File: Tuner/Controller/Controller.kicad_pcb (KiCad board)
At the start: 2 copper layers, 96.8 x 99.3 mm, 169 parts, among them J1 Conn_01x06, J10 Conn_01x05, J11 Conn_01x01, J12 Conn_01x02, J14 Conn_01x01, J15 Conn_01x02, J16 Conn_01x06, J17 Conn_01x01, J18 Conn_01x01, J19 Conn_01x01, J2 Conn_01x06, J20 Conn_01x01, J21 Conn_01x01, J22 Conn_01x06, J23 Conn_01x01, J24 Conn_01x01, J25 Conn_01x01, J26 Conn_01x02, J27 Conn_01x02, J28 Conn_01x02, J3 Conn_01x06, J30 Conn_01x02, J4 Conn_01x06, J5 Conn_01x06, J6 Conn_01x06, J7 Conn_01x02, J8 Conn_01x06, J9 Conn_01x06, Q1 2N3904, Q2 2N3904, Q3 2N3904, Q4 2N3904, Q5 2N3904, Q6 2N3904, Q7 2N3904, Q8 2N3904, U1 74LS393, U2 74HC14, U3 74HC86, U4 LM350_TO220

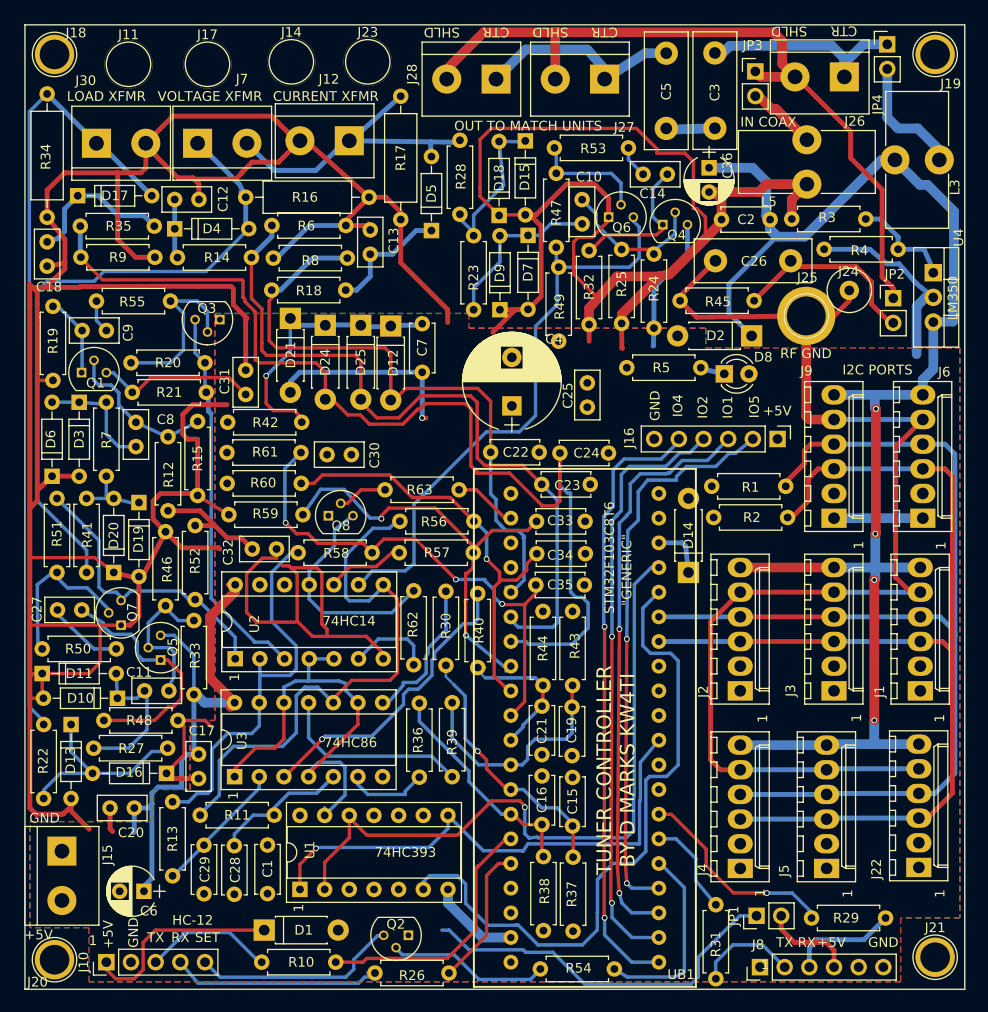
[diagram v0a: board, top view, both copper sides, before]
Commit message: JLCPCB order 09232018 - improved grounding - improved I2C cabling - NEO7M port - support for common mode chokes - relay board now has capacitors on all coils
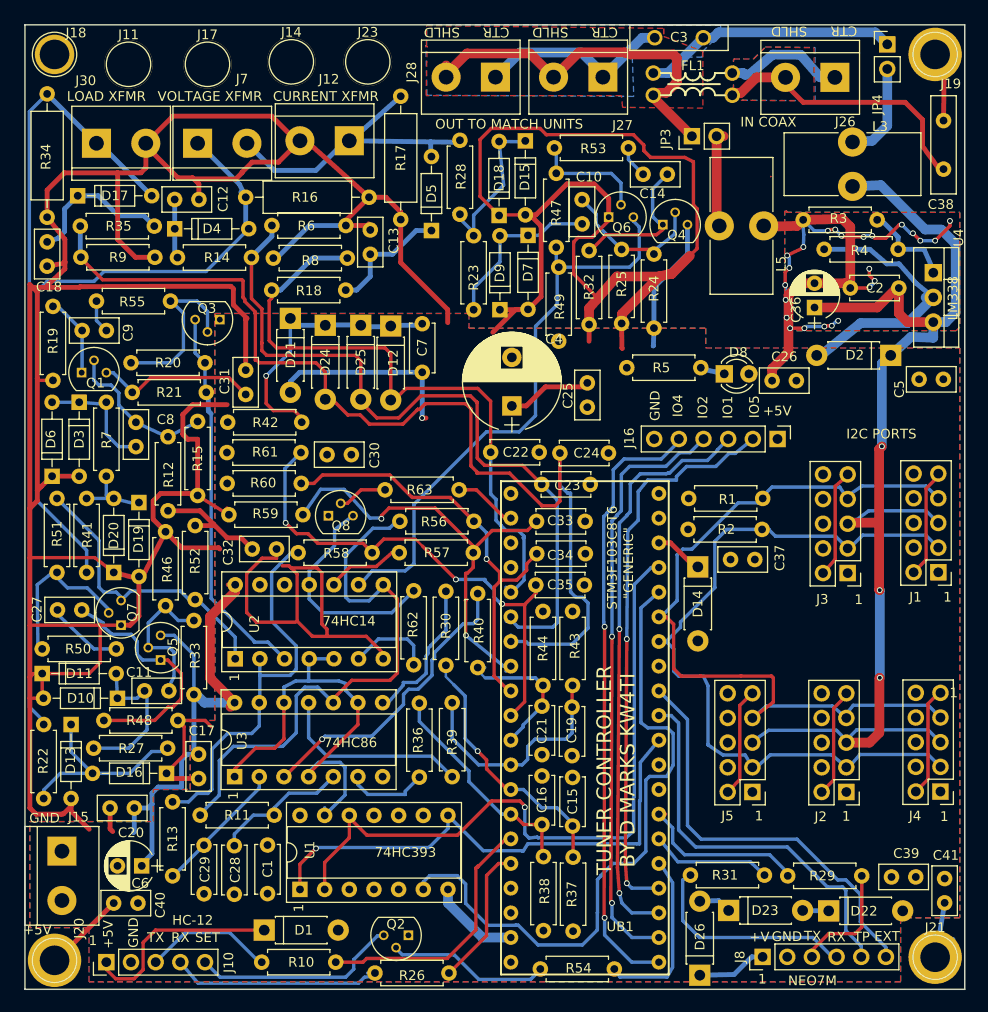
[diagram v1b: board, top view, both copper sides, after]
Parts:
- removed J22, J6, J9: Conn_01x06, Connectors_Molex:Molex_KK-6410-06_06x2.54mm_Straight
- removed J24, J25: Conn_01x01, Connectors:1pin
- removed JP1, JP2: Jumper, Pin_Headers:Pin_Header_Straight_1x02_Pitch2.54mm
- removed R45: 10k, Resistors_THT:R_Axial_DIN0207_L6.3mm_D2.5mm_P7.62mm_Horizontal
- added C37: 0.1 uF, Capacitors_THT:C_Disc_D5.0mm_W2.5mm_P2.50mm, F.Cu at (130.5, 84.0)
- added C38: 0.1 uF, Capacitors_THT:C_Disc_D10.0mm_W2.5mm_P5.00mm, F.Cu at (150.0, 43.8)
- added C39: 0.1 uF, Capacitors_THT:C_Disc_D5.0mm_W2.5mm_P2.50mm, F.Cu at (147.1, 116.7)
- added C40: 0.1 uF, Capacitors_THT:C_Disc_D5.0mm_W2.5mm_P2.50mm, F.Cu at (64.5, 119.4)
- added C41: 0.1 uF, Capacitors_THT:C_Disc_D5.0mm_W2.5mm_P2.50mm, F.Cu at (150.1, 119.4)
- added D22: 1N4001, Diodes_THT:D_DO-41_SOD81_P7.62mm_Horizontal, F.Cu at (138.1, 120.2)
- added D23: 1N4001, Diodes_THT:D_DO-41_SOD81_P7.62mm_Horizontal, F.Cu at (127.8, 120.2)
- added D26: 1N4001, Diodes_THT:D_DO-41_SOD81_P7.62mm_Horizontal, F.Cu at (124.9, 126.8)
- added FL1: Choke, Controller:GenericCMCL, F.Cu at (124.1, 36.5)
- C26, C5: footprint Capacitors_THT:C_Disc_D12.0mm_W4.4mm_P7.75mm -> Capacitors_THT:C_Disc_D5.0mm_W2.5mm_P2.50mm
- C3: footprint Capacitors_THT:C_Disc_D12.0mm_W4.4mm_P7.75mm -> Capacitors_THT:C_Disc_D10.0mm_W2.5mm_P5.00mm
- J1, J2, J3, J4, J5: value Conn_01x06 -> Conn_02x05_Odd_Even; footprint Connectors_Molex:Molex_KK-6410-06_06x2.54mm_Straight -> Pin_Headers:Pin_Header_Straight_2x05_Pitch2.54mm
- moved C5 36.7 mm to (147.4, 65.5), turned to 0 degrees
- moved J4 22.1 mm to (149.6, 107.9), turned to 180 degrees
- moved C36 18.0 mm to (136.7, 58.1), turned to 90 degrees
- moved J2 15.1 mm to (140.0, 108.0), turned to 180 degrees
- moved C2 15.0 mm to (140.4, 56.1)
- moved D2 14.5 mm to (144.5, 63.0)
- moved L5 12.6 mm to (126.9, 49.7), turned to 90 degrees
- moved C26 12.4 mm to (134.8, 65.6)
- moved J1 12.3 mm to (149.4, 85.3), turned to 180 degrees
- moved J3 12.2 mm to (140.1, 85.4), turned to 180 degrees
- moved R31 11.0 mm to (123.9, 116.5), turned to 0 degrees
- moved J5 11.0 mm to (130.3, 108.0), turned to 180 degrees
- moved JP3 9.33 mm to (124.1, 40.4), turned to 90 degrees
- moved L3 9.13 mm to (140.6, 41.0), turned to 0 degrees
- moved R29 4.99 mm to (141.5, 116.6)
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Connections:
- C26 pad 1: Net-(C26-Pad1) -> +5V
- C26 pad 2: RFGND -> GND
- C5 pad 1: Net-(C3-Pad2) -> +5V
- C5 pad 2: Net-(C5-Pad2) -> GND
- J1 pad 4: I2CSDA -> GND
- J1 pad 5: RFGND -> UPWR
- J1 pad 6: UPWR -> GND
- J19 pad 1: (no net) -> Net-(C38-Pad2)
- J2 pad 4: I2CSDA -> GND
- J2 pad 5: RFGND -> UPWR
- J2 pad 6: UPWR -> GND
- J20 pad 1: (no net) -> Net-(C40-Pad1)
- J21 pad 1: (no net) -> Net-(C41-Pad1)
- J26 pad 1: Net-(C3-Pad1) -> Net-(FL1-Pad1)
- J26 pad 2: Net-(J26-Pad2) -> Net-(C38-Pad1)
- J27 pad 1: Net-(C5-Pad2) -> Net-(C3-Pad2)
- J27 pad 2: Net-(J26-Pad2) -> Net-(FL1-Pad4)
- J28 pad 1: Net-(C5-Pad2) -> Net-(C3-Pad2)
- J28 pad 2: Net-(J26-Pad2) -> Net-(FL1-Pad4)
- J3 pad 4: I2CSDA -> GND
- J3 pad 5: RFGND -> UPWR
- J3 pad 6: UPWR -> GND
- J4 pad 4: I2CSDA -> GND
- J4 pad 5: RFGND -> UPWR
- J4 pad 6: UPWR -> GND
- J5 pad 4: I2CSDA -> GND
- J5 pad 5: RFGND -> UPWR
- J5 pad 6: UPWR -> GND
- J8 pad 1: (no net) -> Net-(D26-Pad1)
- J8 pad 2: Net-(J8-Pad2) -> GND
- J8 pad 5: (no net) -> Net-(J8-Pad5)
- J8 pad 6: GND -> Net-(J8-Pad6)
- JP3 pad 1: Net-(J26-Pad2) -> Net-(FL1-Pad4)
- R31 pad 1: Net-(J8-Pad2) -> Net-(J8-Pad4)
- UB1 pad 39: (no net) -> Net-(J8-Pad5)
- UB1 pad 40: (no net) -> Net-(J8-Pad6)
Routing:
- net RFGND: track 128.6 -> 0.00 mm
- net Net-(J26-Pad2): track 78.3 -> 0.00 mm
- net Net-(J8-Pad6): track 0.00 -> 43.7 mm
- net Net-(FL1-Pad4): track 0.00 -> 42.0 mm
- net Net-(J8-Pad5): track 0.00 -> 41.6 mm
- net GND: track 567.5 -> 603.3 mm, vias 1 -> 25
- net +5V: track 161.3 -> 193.8 mm
- net UPWR: track 153.3 -> 124.0 mm, vias 4 -> 3
- net Net-(C38-Pad1): track 0.00 -> 29.2 mm
- net I2CSCL: track 110.6 -> 82.0 mm
- net I2CSDA: track 111.8 -> 83.7 mm
- net Net-(C5-Pad2): track 22.3 -> 0.00 mm
- net Net-(C26-Pad1): track 20.2 -> 0.00 mm
- net Net-(C3-Pad2): track 5.06 -> 21.5 mm
- net Net-(FL1-Pad1): track 0.00 -> 15.5 mm
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- added copper zone on F.Cu, net +5V
- added copper zone on B.Cu, net GND
- added copper zone on B.Cu, net Net-(C3-Pad2)
- added copper zone on F.Cu, net Net-(C38-Pad1)
- added copper zone on B.Cu, net Net-(FL1-Pad1)
- added copper zone on F.Cu, net Net-(FL1-Pad4)
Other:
- board text added: "+V"
- board text added: "EXT"
- board text added: "LM338"
- board text added: "NEO7M"
- board text added: "TP"
- board text removed: "LM350"
- board text removed: "RF GND"

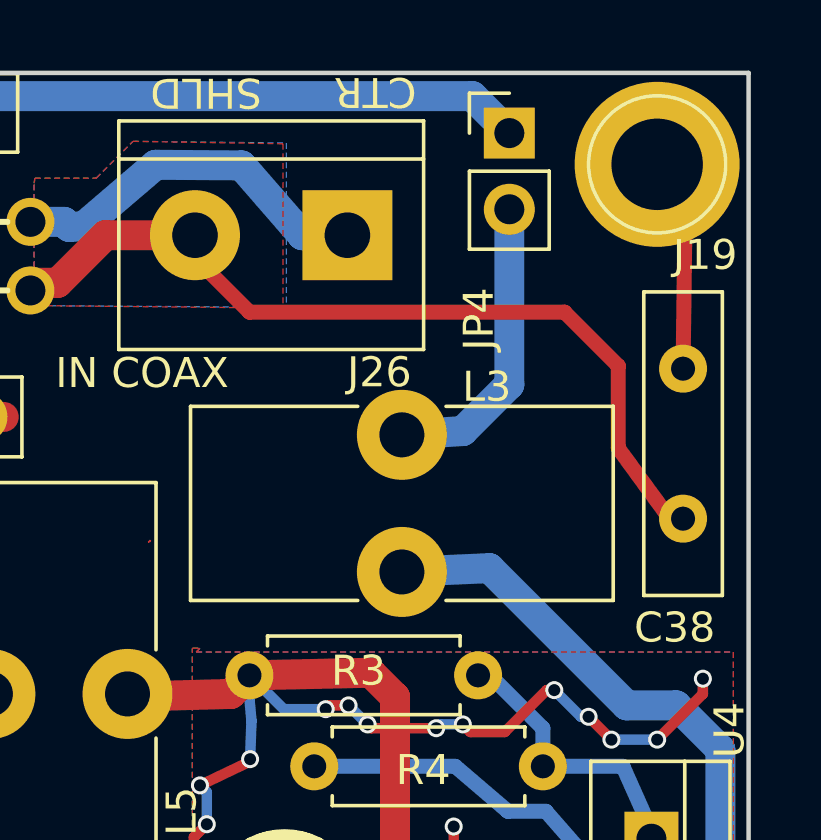
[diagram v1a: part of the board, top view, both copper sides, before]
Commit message: Relay boards changed to have coil terminals all on same side
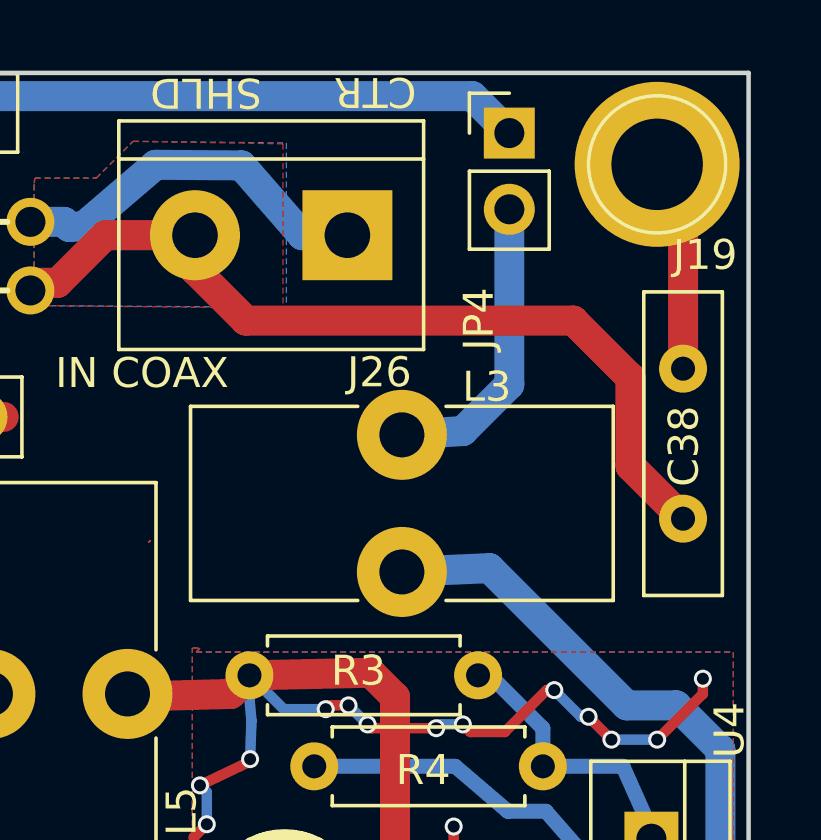
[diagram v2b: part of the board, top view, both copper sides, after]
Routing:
- net Net-(C38-Pad1): track 29.2 -> 30.5 mm
- net Net-(C38-Pad2): track 9.00 -> 10.3 mm
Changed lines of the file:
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@@
     (links 353)
     (no_connects 0)
-    (area 53.127 26.7545 157.029022 130.223619)
+    (area 55.296999 28.880999 152.221001 128.345001)
     (thickness 1.6)
     (drawings 53)
-    (tracks 1544)
+    (tracks 1546)
     (zones 0)
     (modules 170)
@@
   )
   (setup
-    (last_trace_width 0.25)
+    (last_trace_width 1)
     (user_trace_width 0.35)
     (user_trace_width 0.5)
@@
     (descr "C, Disc series, Radial, pin pitch=5.00mm, , diameter*width=10*2.5mm^2, Capacitor, http://cdn-reichelt.de/documents/datenblatt/B300/DS_KERKO_TC.pdf")
     (tags "C Disc series Radial pin pitch 5.00mm  diameter 10mm width 2.5mm Capacitor")
-    (fp_text reference C38 (at -3.6322 -0.2794 180) (layer F.SilkS)
+    (fp_text reference C38 (at 2.413 0.0254 270) (layer F.SilkS)
       (effects (font (size 1 1) (thickness 0.15)))
     )
@@
   (segment (start 149.1742 124.8918) (end 149.098 124.968) (width 0.5) (layer B.Cu) (net 92))
   (segment (start 150.93696 123.12904) (end 149.098 124.968) (width 0.5) (layer B.Cu) (net 92) (status 30))
+  (segment (start 133.6929 34.3662) (end 133.6929 35.5219) (width 1) (layer F.Cu) (net 93) (status C00000))
+  (segment (start 133.6929 35.5219) (end 135.382 37.211) (width 1) (layer F.Cu) (net 93) (status 400000))
+  (segment (start 148.209 42.0624) (end 149.9616 43.815) (width 1) (layer F.Cu) (net 93) (status 800000))
+  (segment (start 148.209 39.116) (end 148.209 42.0624) (width 1) (layer F.Cu) (net 93))
+  (segment (start 146.304 37.211) (end 148.209 39.116) (width 1) (layer F.Cu) (net 93))
+  (segment (start 135.382 37.211) (end 146.304 37.211) (width 1) (layer F.Cu) (net 93))
   (segment (start 133.6929 34.3662) (end 133.6929 35.1155) (width 0.5) (layer F.Cu) (net 93))
-  (segment (start 133.6929 35.1155) (end 135.509 36.9316) (width 0.5) (layer F.Cu) (net 93))
-  (segment (start 147.8026 41.4655) (end 149.5171 43.815) (width 0.5) (layer F.Cu) (net 93) (status 20))
-  (segment (start 147.8026 38.7223) (end 147.8026 41.4655) (width 0.5) (layer F.Cu) (net 93))
-  (segment (start 146.0119 36.9316) (end 147.8026 38.7223) (width 0.5) (layer F.Cu) (net 93))
-  (segment (start 135.509 36.9316) (end 146.0119 36.9316) (width 0.5) (layer F.Cu) (net 93))
   (segment (start 149.5171 43.815) (end 149.9616 43.815) (width 0.5) (layer F.Cu) (net 93) (status 30))
   (segment (start 133.6929 34.3662) (end 133.6929 34.8234) (width 0.5) (layer F.Cu) (net 93) (status 30))
@@
   (segment (start 130.70332 34.3662) (end 129.11582 35.9537) (width 1) (layer F.Cu) (net 93))
   (segment (start 133.7945 34.3662) (end 133.6929 34.3662) (width 0.5) (layer F.Cu) (net 93) (status 30))
-  (segment (start 149.9616 38.815) (end 150.0378 32.9438) (width 0.5) (layer F.Cu) (net 94) (status 10))
+  (segment (start 149.9616 38.815) (end 149.9616 32.8676) (width 1) (layer F.Cu) (net 94) (status C00000))
+  (segment (start 149.9616 32.8676) (end 149.098 32.004) (width 1) (layer F.Cu) (net 94) (status C00000))
   (segment (start 150.0378 32.9438) (end 149.098 32.004) (width 0.5) (layer F.Cu) (net 94))
   (segment (start 150.368 33.274) (end 149.098 32.004) (width 0.5) (layer F.Cu) (net 94) (status 30))

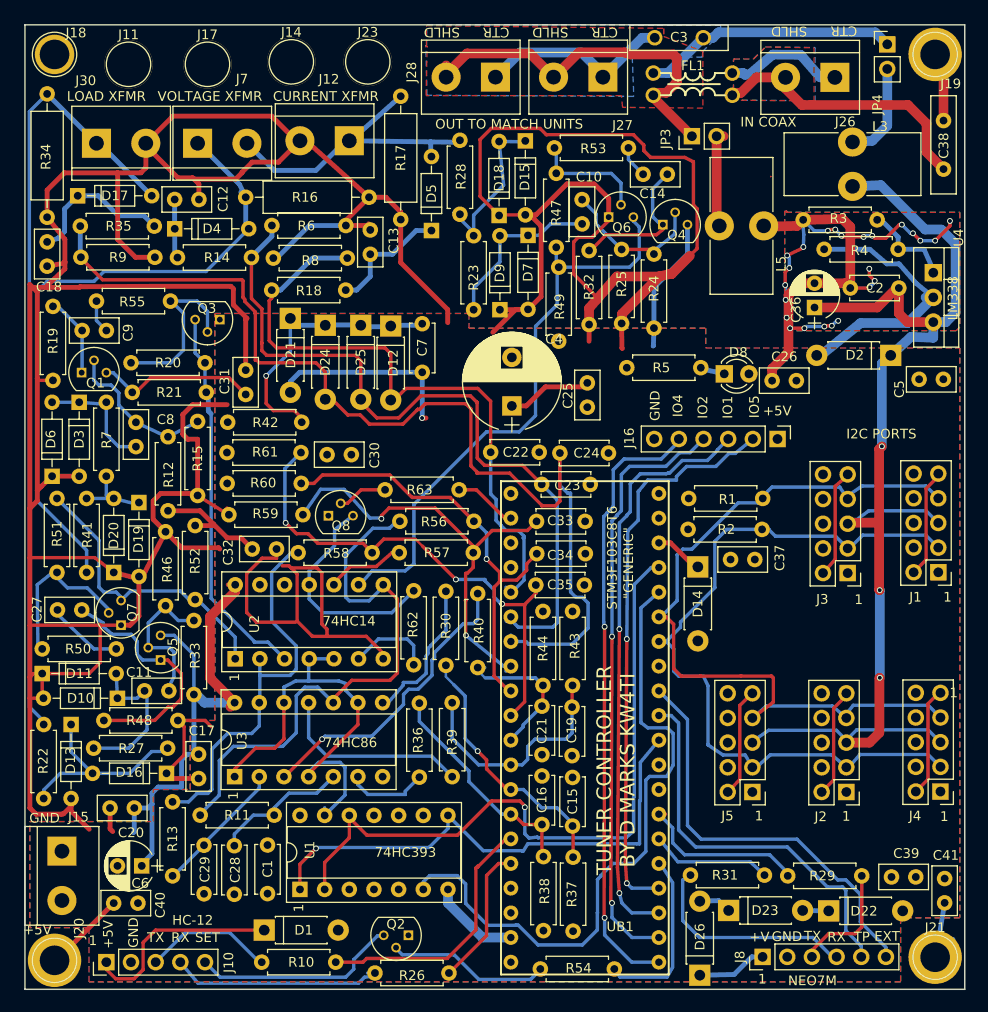
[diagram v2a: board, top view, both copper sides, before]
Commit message: Added boards for SMIH/Schrack Relays
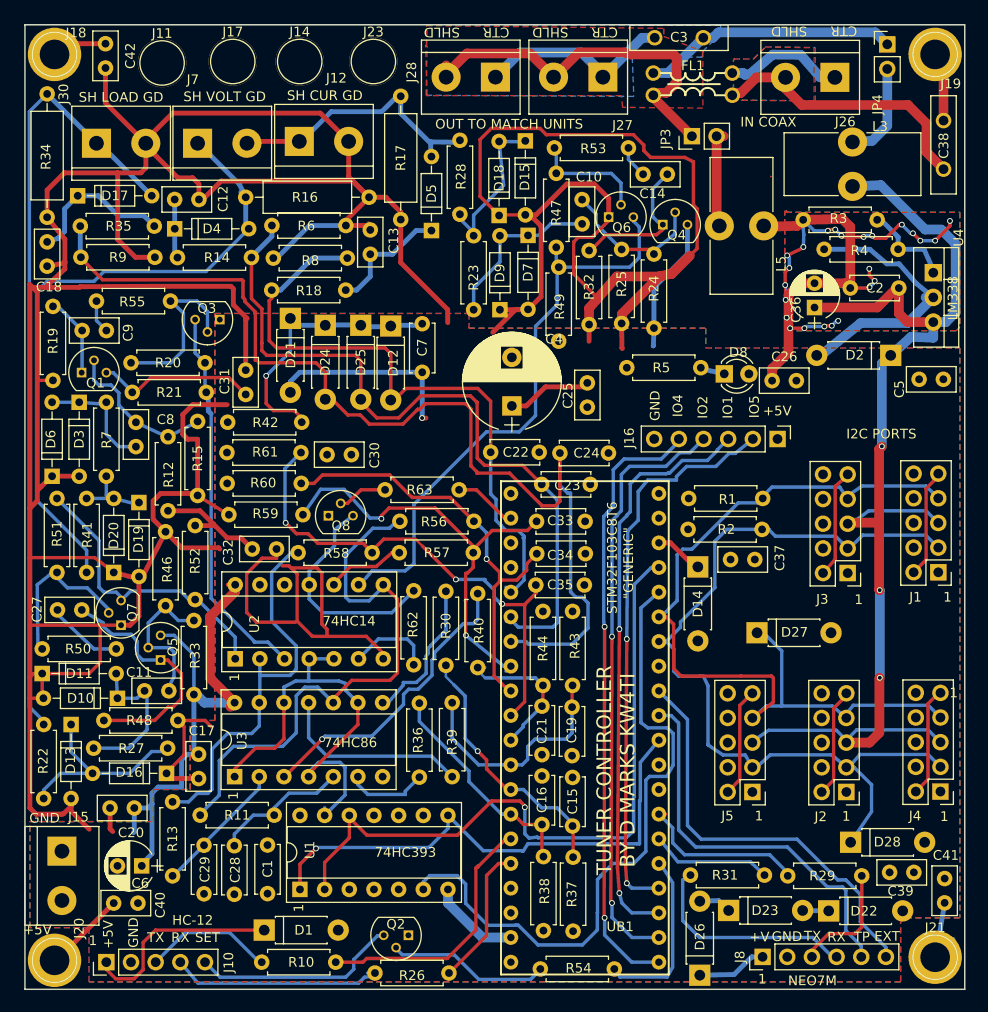
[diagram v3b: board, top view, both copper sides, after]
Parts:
- added C42: 0.1 uF, Capacitors_THT:C_Disc_D5.0mm_W2.5mm_P2.50mm, F.Cu at (63.7, 30.9)
- added D27: 1N4733A, Diodes_THT:D_DO-41_SOD81_P7.62mm_Horizontal, F.Cu at (130.8, 91.6)
- added D28: 1N4733A, Diodes_THT:D_DO-41_SOD81_P7.62mm_Horizontal, F.Cu at (140.4, 113.1)
- moved J12 5.15 mm to (83.6, 41.0), turned to 0 degrees
- moved J11 3.46 mm to (69.5, 32.9)
- moved J17 2.62 mm to (76.8, 32.7)
- moved J14 0.86 mm to (83.7, 32.7)
- moved J23 0.58 mm to (91.3, 32.7)
- moved C39 0.51 mm to (146.9, 116.2)
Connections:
- J18 pad 1: (no net) -> Net-(C42-Pad1)
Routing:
- net GND: track 603.3 -> 622.4 mm
- net I2CSCL: track 82.0 -> 91.9 mm
- net I2CSDA: track 83.7 -> 92.7 mm
- net Net-(C42-Pad1): track 0.00 -> 5.70 mm
- net XRev: track 33.8 -> 28.6 mm
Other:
- board text added: "SH CUR GD"
- board text added: "SH LOAD GD"
- board text added: "SH VOLT GD"
- board text removed: "CURRENT XFMR"
- board text removed: "LOAD XFMR"
- board text removed: "VOLTAGE XFMR"
